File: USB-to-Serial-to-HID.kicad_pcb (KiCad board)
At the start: 2 copper layers, 43.8 x 17.5 mm, 14 parts, among them J2 USB4520-03-1-A, J3 48037-2200, U1 CH340C, U2 CH9329

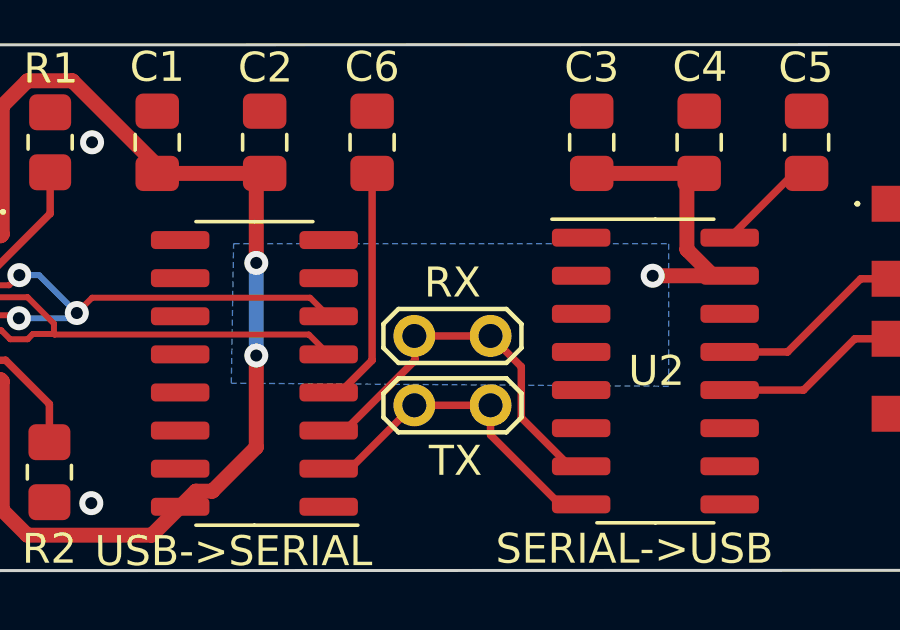
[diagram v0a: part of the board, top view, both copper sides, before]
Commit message: Update 480372200.kicad_mod and PCB
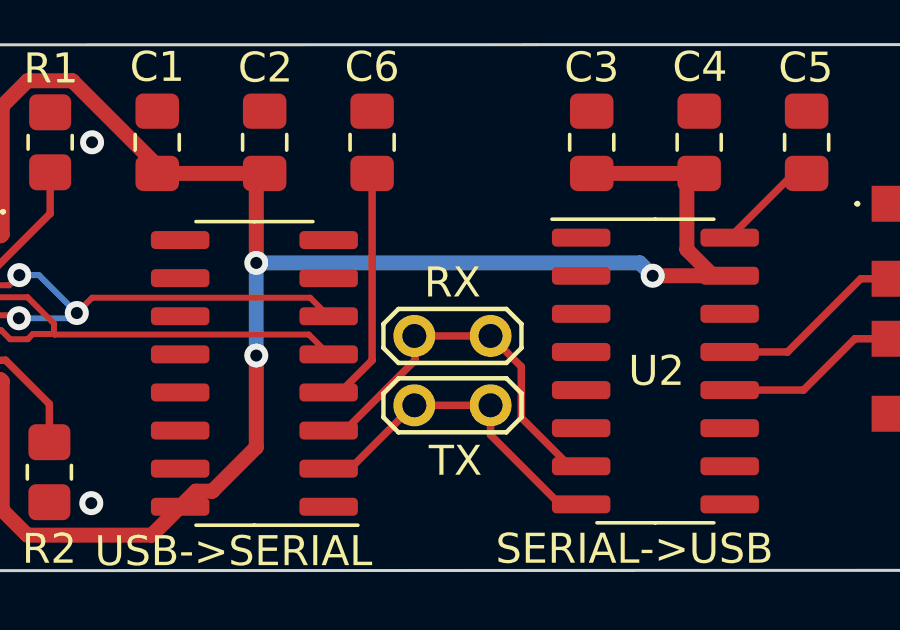
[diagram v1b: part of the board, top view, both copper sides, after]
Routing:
- net USB_VIN: track 51.3 -> 64.6 mm
- removed copper zone on B.Cu, net USB_VIN
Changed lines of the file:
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@@
     (pad "MH2" thru_hole circle (at -5.85 -7.575 90) (size 3.9 3.9) (drill 2.6) (layers "*.Cu" "*.Mask")
       (net 11 "GND") (pinfunction "MH2") (pintype "passive"))
-    (model "${KIPRJMOD}/LibraryLoader/SamacSys_Parts.3dshapes/48037-2200.stp"
+    (model "C:\\Users\\James Allerton\\Documents\\USB HID\\LibraryLoader\\SamacSys_Parts.3dshapes\\48037-2200.stp"
       (offset (xyz 0 -0.6000000148 -0.239999991))
       (scale (xyz 1 1 1))
@@
   (via (at 120.4158 73.283) (size 0.8) (drill 0.4) (layers "F.Cu" "B.Cu") (net 20))
   (segment (start 120.4158 73.283) (end 120.4158 76.2548) (width 0.5) (layer "B.Cu") (net 20))
+  (segment (start 133.2016 73.283) (end 133.6294 73.7108) (width 0.5) (layer "B.Cu") (net 20))
+  (segment (start 120.4158 73.283) (end 133.2016 73.283) (width 0.5) (layer "B.Cu") (net 20))
   (segment (start 140.565 73.811) (end 141.926 73.811) (width 0.25) (layer "F.Cu") (net 21))
   (segment (start 138.1252 76.2508) (end 140.565 73.811) (width 0.25) (layer "F.Cu") (net 21))
@@
       )
     )
-  )
-  (zone (net 20) (net_name "USB_VIN") (layer "B.Cu") (hatch edge 0.5)
-    (connect_pads (clearance 0.2))
-    (min_thickness 0.25) (filled_areas_thickness no)
-    (fill yes (thermal_gap 0.5) (thermal_bridge_width 0.5))
-    (polygon
-      (pts
-        (xy 134.1628 72.644)
-        (xy 134.1628 77.3938)
-        (xy 119.5832 77.2922)
-        (xy 119.6594 72.644)
-        (xy 120.142 72.644)
-      )
-    )
